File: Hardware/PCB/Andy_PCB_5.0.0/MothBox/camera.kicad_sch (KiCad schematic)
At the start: 0 parts

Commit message: added female inverted header
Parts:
- added B1: ~, AQLibrary:Talentcell, symbol AQ_Library_0:Talentcell
- added H1, H2, H3, H4, H5, H6, H7, H8: MountingHole_1/4inbolt, MountingHole:MountingHole_6.4mm_M6_Pad, symbol AQ_Library_0:MountingHole_1/4inbolt
- added U14: ~, Attractor:Arducam Owlsight, symbol attractor:camera2

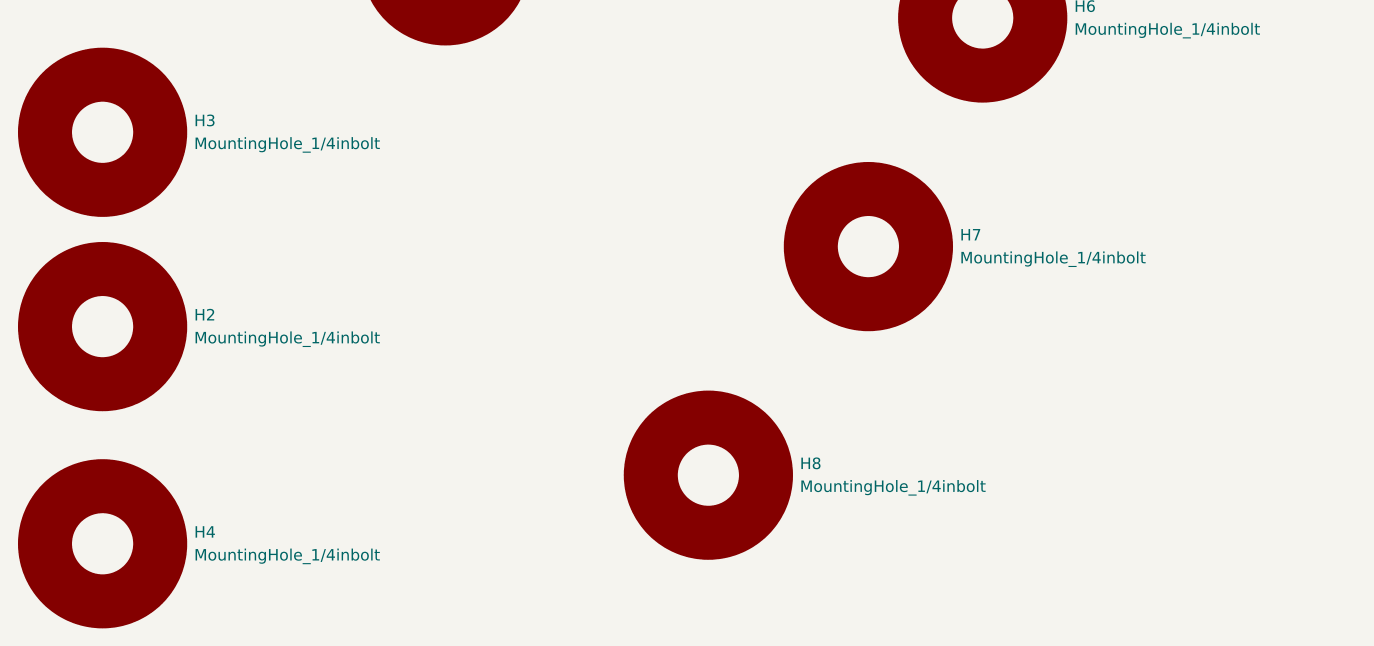
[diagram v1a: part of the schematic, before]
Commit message: Tweaked Mothbeam and added GPS footprints
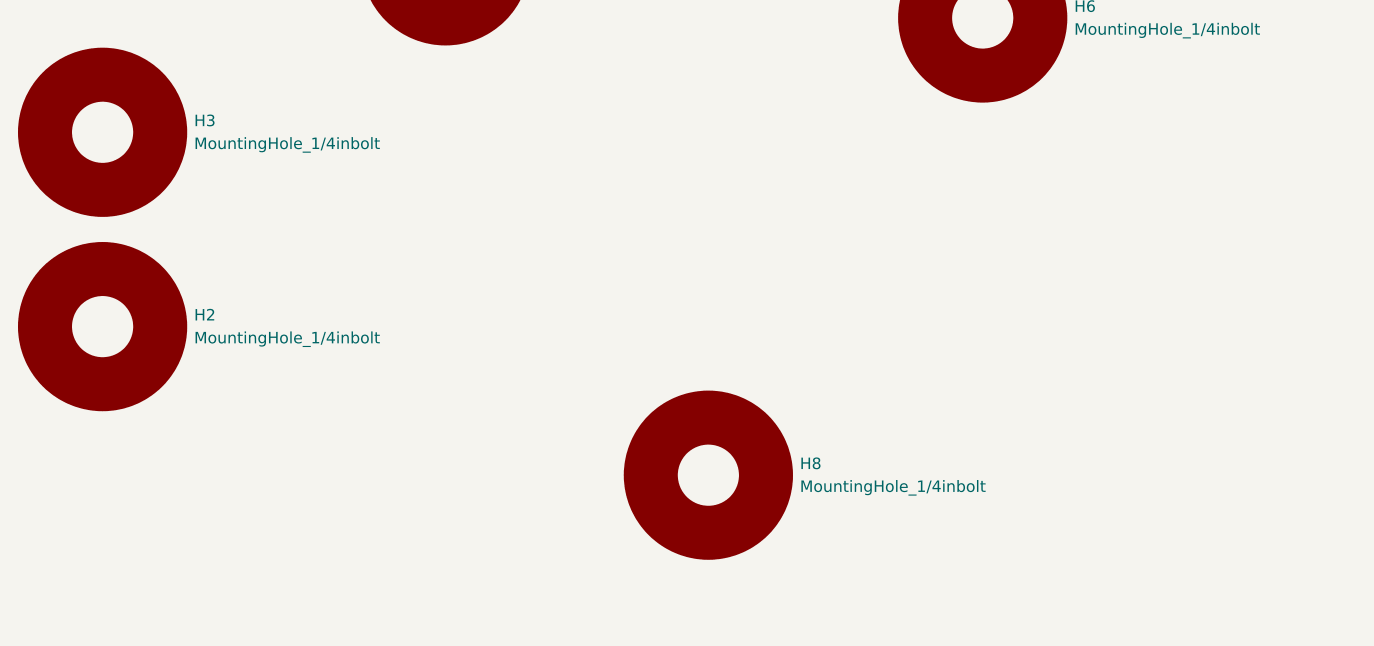
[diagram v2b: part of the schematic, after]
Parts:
- removed H4, H7: MountingHole_1/4inbolt, MountingHole:MountingHole_6.4mm_M6_Pad, symbol AQ_Library_0:MountingHole_1/4inbolt
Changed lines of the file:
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@@
-	(symbol
-		(lib_id "AQ_Library_0:MountingHole_1/4inbolt")
-		(at 115.57 116.84 0)
-		(unit 1)
-		(exclude_from_sim no)
-		(in_bom no)
-		(on_board yes)
-		(dnp no)
-		(fields_autoplaced yes)
-		(property "Reference" "H7"
-			(at 125.73 115.5699 0)
-			(effects
-				(font
-					(size 1.27 1.27)
-				)
-				(justify left)
-			)
-		)
-		(property "Value" "MountingHole_1/4inbolt"
-			(at 125.73 118.1099 0)
-			(effects
-				(font
-					(size 1.27 1.27)
-				)
-				(justify left)
-			)
-		)
-		(property "Footprint" "MountingHole:MountingHole_6.4mm_M6_Pad"
-			(at 115.57 116.84 0)
-			(effects
-				(font
-					(size 1.27 1.27)
-				)
-				(hide yes)
-			)
-		)
-		(property "Datasheet" "~"
-			(at 115.57 116.84 0)
-			(effects
-				(font
-					(size 1.27 1.27)
-				)
-				(hide yes)
-			)
-		)
-		(property "Description" "Mounting Hole without connection"
-			(at 115.57 116.84 0)
-			(effects
-				(font
-					(size 1.27 1.27)
-				)
-				(hide yes)
-			)
-		)
-		(instances
-			(project "MothBox"
-				(path "/9021e528-fc76-4423-a3f3-30f5652071cc/84c07412-33ce-4c0b-96a0-a76ad52e50ee"
-					(reference "H7")
-					(unit 1)
-				)
-			)
-		)
-	)
 	(symbol
 		(lib_id "AQ_Library_0:MountingHole_1/4inbolt")
@@
 					(unit 1)
 				)
-			)
-		)
-	)
-	(symbol
-		(lib_id "AQ_Library_0:MountingHole_1/4inbolt")
-		(at 30.48 149.86 0)
-		(unit 1)
-		(exclude_from_sim no)
-		(in_bom no)
-		(on_board yes)
-		(dnp no)
-		(fields_autoplaced yes)
-		(property "Reference" "H4"
-			(at 40.64 148.5899 0)
-			(effects
-				(font
-					(size 1.27 1.27)
-				)
-				(justify left)
-			)
-		)
-		(property "Value" "MountingHole_1/4inbolt"
-			(at 40.64 151.1299 0)
-			(effects
-				(font
-					(size 1.27 1.27)
-				)
-				(justify left)
-			)
-		)
-		(property "Footprint" "MountingHole:MountingHole_6.4mm_M6_Pad"
-			(at 30.48 149.86 0)
-			(effects
-				(font
-					(size 1.27 1.27)
-				)
-				(hide yes)
-			)
-		)
-		(property "Datasheet" "~"
-			(at 30.48 149.86 0)
-			(effects
-				(font
-					(size 1.27 1.27)
-				)
-				(hide yes)
-			)
-		)
-		(property "Description" "Mounting Hole without connection"
-			(at 30.48 149.86 0)
-			(effects
-				(font
-					(size 1.27 1.27)
-				)
-				(hide yes)
-			)
-		)
-		(instances
-			(project "MothBox"
-				(path "/9021e528-fc76-4423-a3f3-30f5652071cc/84c07412-33ce-4c0b-96a0-a76ad52e50ee"
-					(reference "H4")
-					(unit 1)
-				)

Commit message: Fixed parts with conflicting LCSC footprints
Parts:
- U14: now left out of the parts list
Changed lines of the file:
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@@
 		(unit 1)
 		(exclude_from_sim no)
-		(in_bom yes)
+		(in_bom no)
 		(on_board yes)
 		(dnp no)
@@
 		(at 204.47 36.83 0)
 		(unit 1)
-		(exclude_from_sim no)
-		(in_bom no)
-		(on_board yes)
+		(exclude_from_sim yes)
+		(in_bom no)
+		(on_board yes)

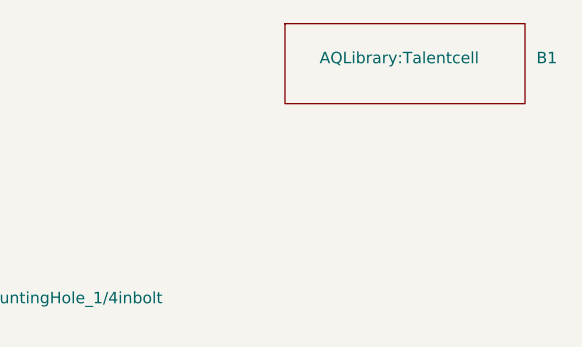
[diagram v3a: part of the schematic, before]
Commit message: Final changes footprints before JLC
c1 - rotate left 180

e3 - rotate left 180

q1 rotate l 180

U1,U2,U6,U7 rotate 180

u5 Epaper header - 90 right

u16 - NOT RIGHT ANGLE should be C2897440  or C22373943
d30 they might be bidirectional

Q10,Q11,Q4,Q6,Q8,Q9

C39828
rotate 180
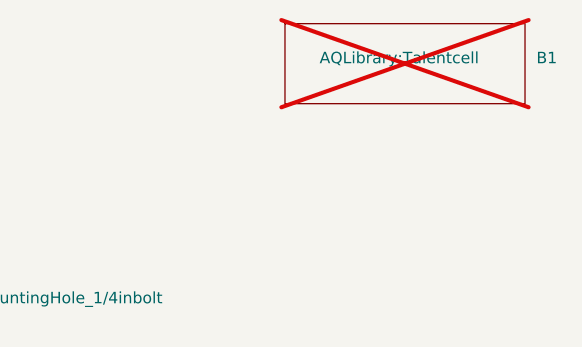
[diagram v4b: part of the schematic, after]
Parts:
- B1: now not fitted
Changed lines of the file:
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@@
 		(in_bom no)
 		(on_board yes)
-		(dnp no)
+		(dnp yes)
 		(fields_autoplaced yes)
 		(property "Reference" "B1"

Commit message: Maybe these files needed saving too for paul?
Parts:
- B1: symbol AQ_Library_0:Talentcell -> MB_Library:Talentcell
- H1, H2, H3, H5, H6, H8: symbol AQ_Library_0:MountingHole_1/4inbolt -> MB_Library:MountingHole_1/4inbolt
- U14: symbol attractor:camera2 -> MB_Library:camera2
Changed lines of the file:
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@@
 	(paper "A4")
 	(symbol
-		(lib_id "AQ_Library_0:MountingHole_1/4inbolt")
+		(lib_id "MB_Library:MountingHole_1/4inbolt")
 		(at 68.58 85.09 0)
 		(unit 1)
@@
 	)
 	(symbol
-		(lib_id "AQ_Library_0:MountingHole_1/4inbolt")
+		(lib_id "MB_Library:MountingHole_1/4inbolt")
 		(at 97.79 142.24 0)
 		(unit 1)
@@
 	)
 	(symbol
-		(lib_id "attractor:camera2")
+		(lib_id "MB_Library:camera2")
 		(at 68.58 40.64 0)
 		(unit 1)
@@
 	)
 	(symbol
-		(lib_id "AQ_Library_0:MountingHole_1/4inbolt")
+		(lib_id "MB_Library:MountingHole_1/4inbolt")
 		(at 30.48 104.14 0)
 		(unit 1)
@@
 	)
 	(symbol
-		(lib_id "AQ_Library_0:MountingHole_1/4inbolt")
+		(lib_id "MB_Library:MountingHole_1/4inbolt")
 		(at 30.48 125.73 0)
 		(unit 1)
@@
 	)
 	(symbol
-		(lib_id "AQ_Library_0:MountingHole_1/4inbolt")
+		(lib_id "MB_Library:MountingHole_1/4inbolt")
 		(at 147.32 62.23 0)
 		(unit 1)
@@
 	)
 	(symbol
-		(lib_id "AQ_Library_0:MountingHole_1/4inbolt")
+		(lib_id "MB_Library:MountingHole_1/4inbolt")
 		(at 128.27 91.44 0)
 		(unit 1)
@@
 	)
 	(symbol
-		(lib_id "AQ_Library_0:Talentcell")
+		(lib_id "MB_Library:Talentcell")
 		(at 204.47 36.83 0)
 		(unit 1)
